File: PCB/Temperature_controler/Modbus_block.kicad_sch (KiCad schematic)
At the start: 0 parts

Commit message: PCB progress
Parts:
- added C44, C45: 100nF, Capacitor_SMD:C_0805_2012Metric_Pad1.18x1.45mm_HandSolder, symbol Device:C
- added C46, C47: 0,1µF, Capacitor_SMD:C_0805_2012Metric_Pad1.18x1.45mm_HandSolder, symbol Device:C
- added J6: A/B IN, TerminalBlock_Phoenix:TerminalBlock_Phoenix_MKDS-1,5-2_1x02_P5.00mm_Horizontal, symbol Connector:Screw_Terminal_01x02
- added R20, R21, R24: 10kΩ, Resistor_SMD:R_0805_2012Metric_Pad1.20x1.40mm_HandSolder, symbol Device:R
- added R22, R23: 10Ω, Resistor_SMD:R_0805_2012Metric_Pad1.20x1.40mm_HandSolder, symbol Device:R
- added U10: TXB0104PWR, TXB0104PWR:PW14, symbol TXB0104PWR:TXB0104PWR
- added U8: SN65HVD485EP, SN65HVD485EP:P8, symbol SN65HVD485EP:SN65HVD485EP
- added U9: CDSOT23-SM712, CDSOT23-SM712:SOT_SM712, symbol CDSOT23-SM712:CDSOT23-SM712
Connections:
- new net: C45.1, R20.1, U10.11 (B3), U8.1 (R)
- new net: R21.2, U10.12 (B2), U8.2 (*RE), U8.3 (DE)
- new net: U10.13 (B1), U8.4 (D)
- new net: R23.2, U8.6 (A)
- new net: R22.2, U8.7 (B)
- new net: J6.2 (Pin_2), R22.1, U9.3
- new net: J6.1 (Pin_1), R23.1, U9.2
- new net: R24.1, U10.8 (OE)
- new net +3.3V: C46.2, U10.1 (VCCA)
- new net +5V: C44.1, C47.2, R20.2, U10.14 (VCCB), U8.8 (VCC)
- new net GND: C44.2, C45.2, C46.1, C47.1, R21.1, R24.2, U10.7 (GND), U8.5 (GND), U9.1
- new net RS485_DIR: U10.3 (A2)
- new net RS485_RX: U10.4 (A3)
- new net RS485_Tx: U10.2 (A1)

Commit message: Schematic update, PCB progress
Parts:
- added R29: 10Ω, Resistor_SMD:R_0805_2012Metric_Pad1.20x1.40mm_HandSolder, symbol Device:R
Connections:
- net GND: now also U9.3; no longer U9.1
- net RS485_RX: now also U10.2 (A1); no longer U10.4 (A3)
- net RS485_Tx: now also U10.5 (A4); no longer U10.2 (A1)
- net at C45.1, R20.1, U8.1 (R): now also U10.13 (B1); no longer U10.11 (B3)
- net at U8.4 (D): now also U10.10 (B4); no longer U10.13 (B1)
- net at J6.2 (Pin_2), R22.1: now also U9.2, R29.1; no longer U9.3
- net at J6.1 (Pin_1), R23.1: now also U9.1, R29.2; no longer U9.2
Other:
- moved on the sheet: J6, R22, R23, U9

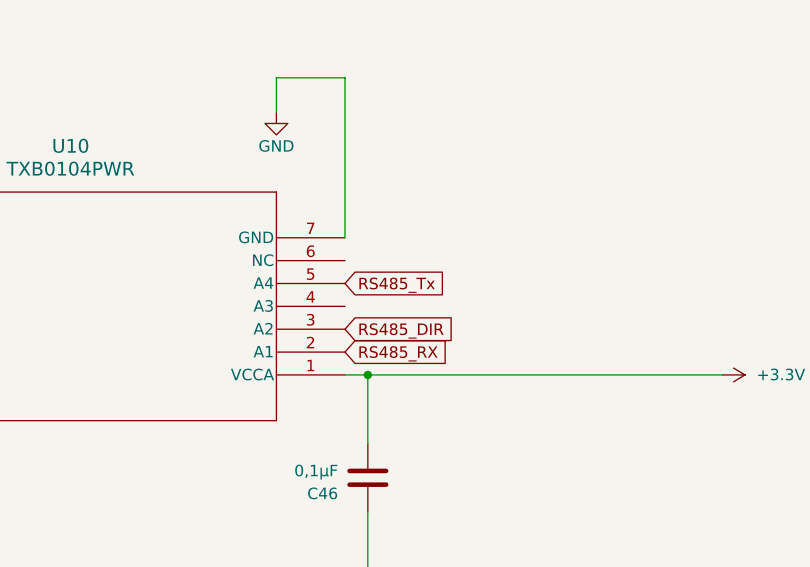
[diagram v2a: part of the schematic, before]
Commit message: PCB traces changed
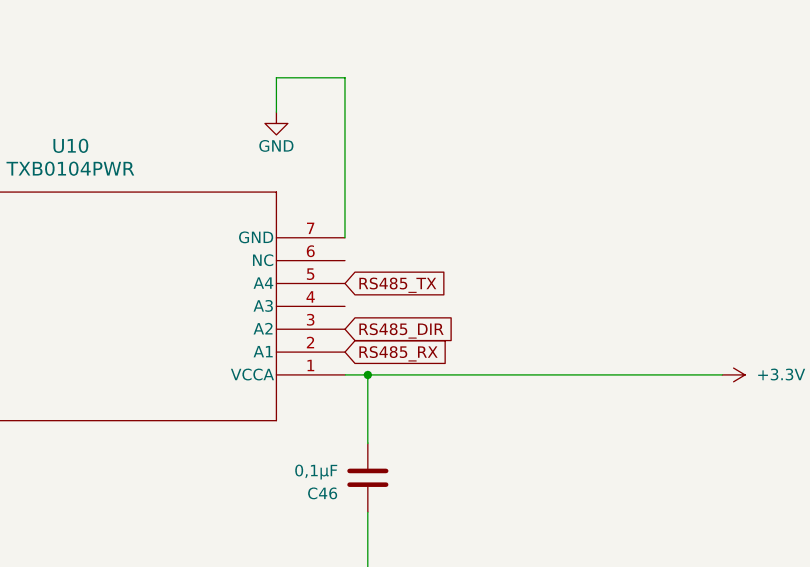
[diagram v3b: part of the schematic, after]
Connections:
- net RS485_Tx renamed RS485_TX
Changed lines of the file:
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@@
 		)
 	)
-	(global_label "RS485_Tx"
+	(global_label "RS485_TX"
 		(shape input)
 		(at 166.37 125.73 0)
@@
 		)
 		(property "Intersheetrefs" "${INTERSHEET_REFS}"
-			(at 178.4265 125.73 0)
+			(at 178.6079 125.73 0)
 			(effects
 				(font
